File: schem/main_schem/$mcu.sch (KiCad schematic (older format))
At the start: 36 parts, among them P2 CONN_PORTD, P3 CONN_ICD, P4 CONN_NFC, SW1 SW_RESET, U4 25LC256, U5 PIC18F97J60, X1 25MHz

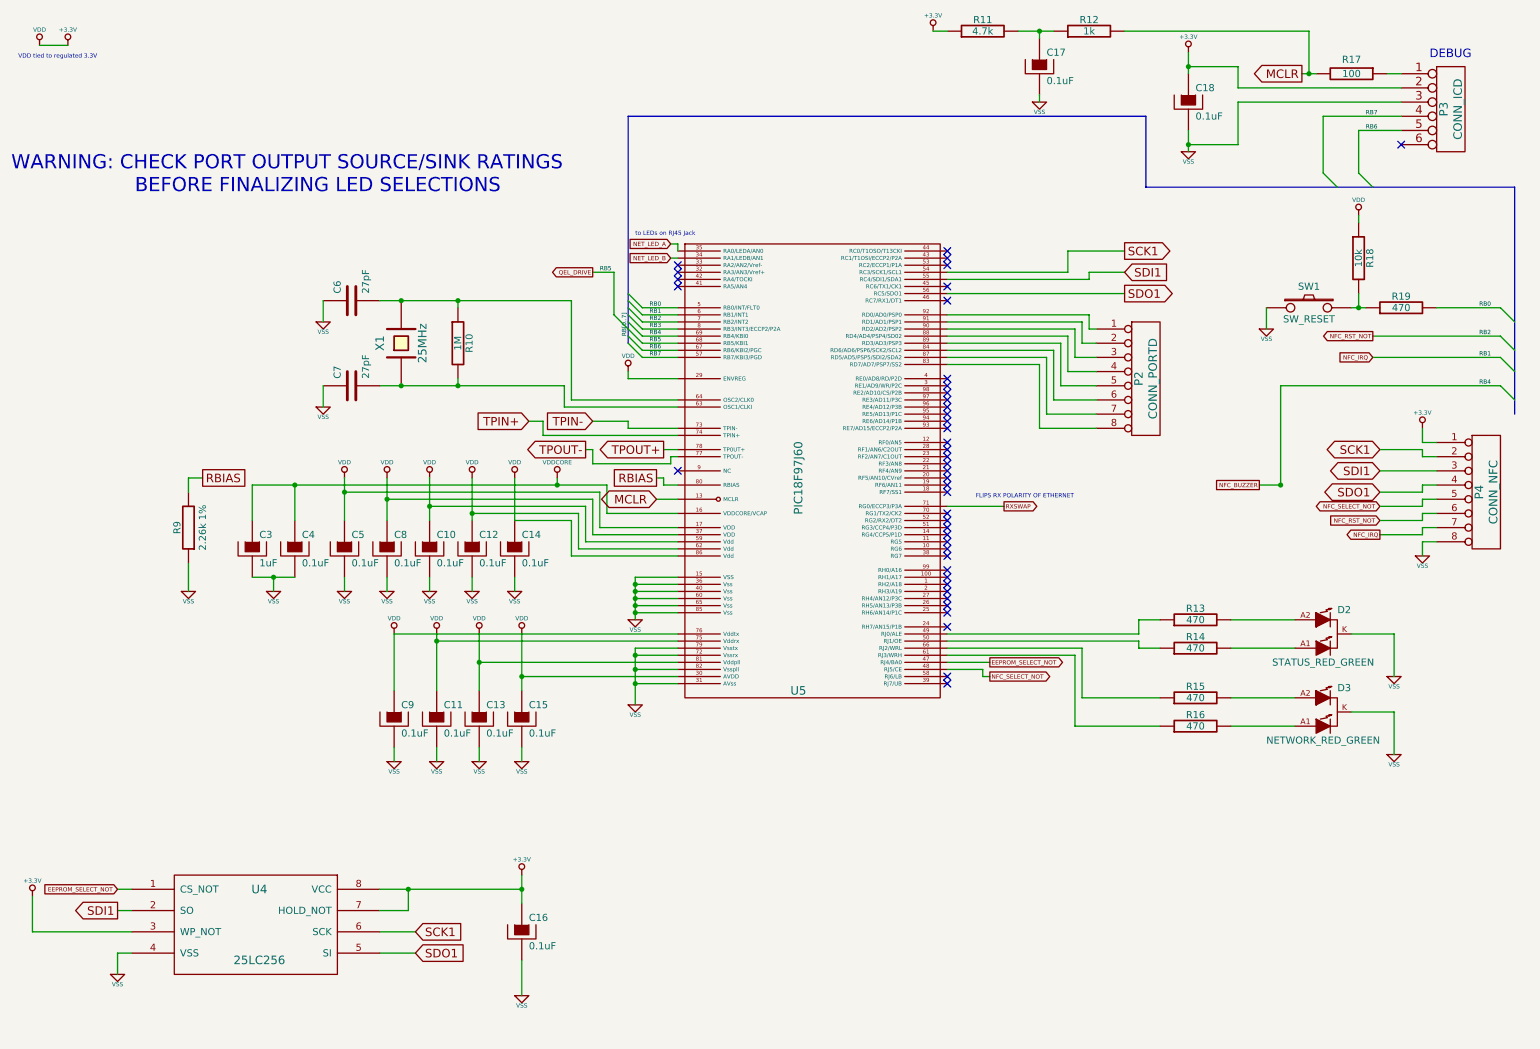
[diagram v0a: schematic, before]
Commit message: Board has own RJ45 jack, finish nearly all logic of board, add QELink screenprint
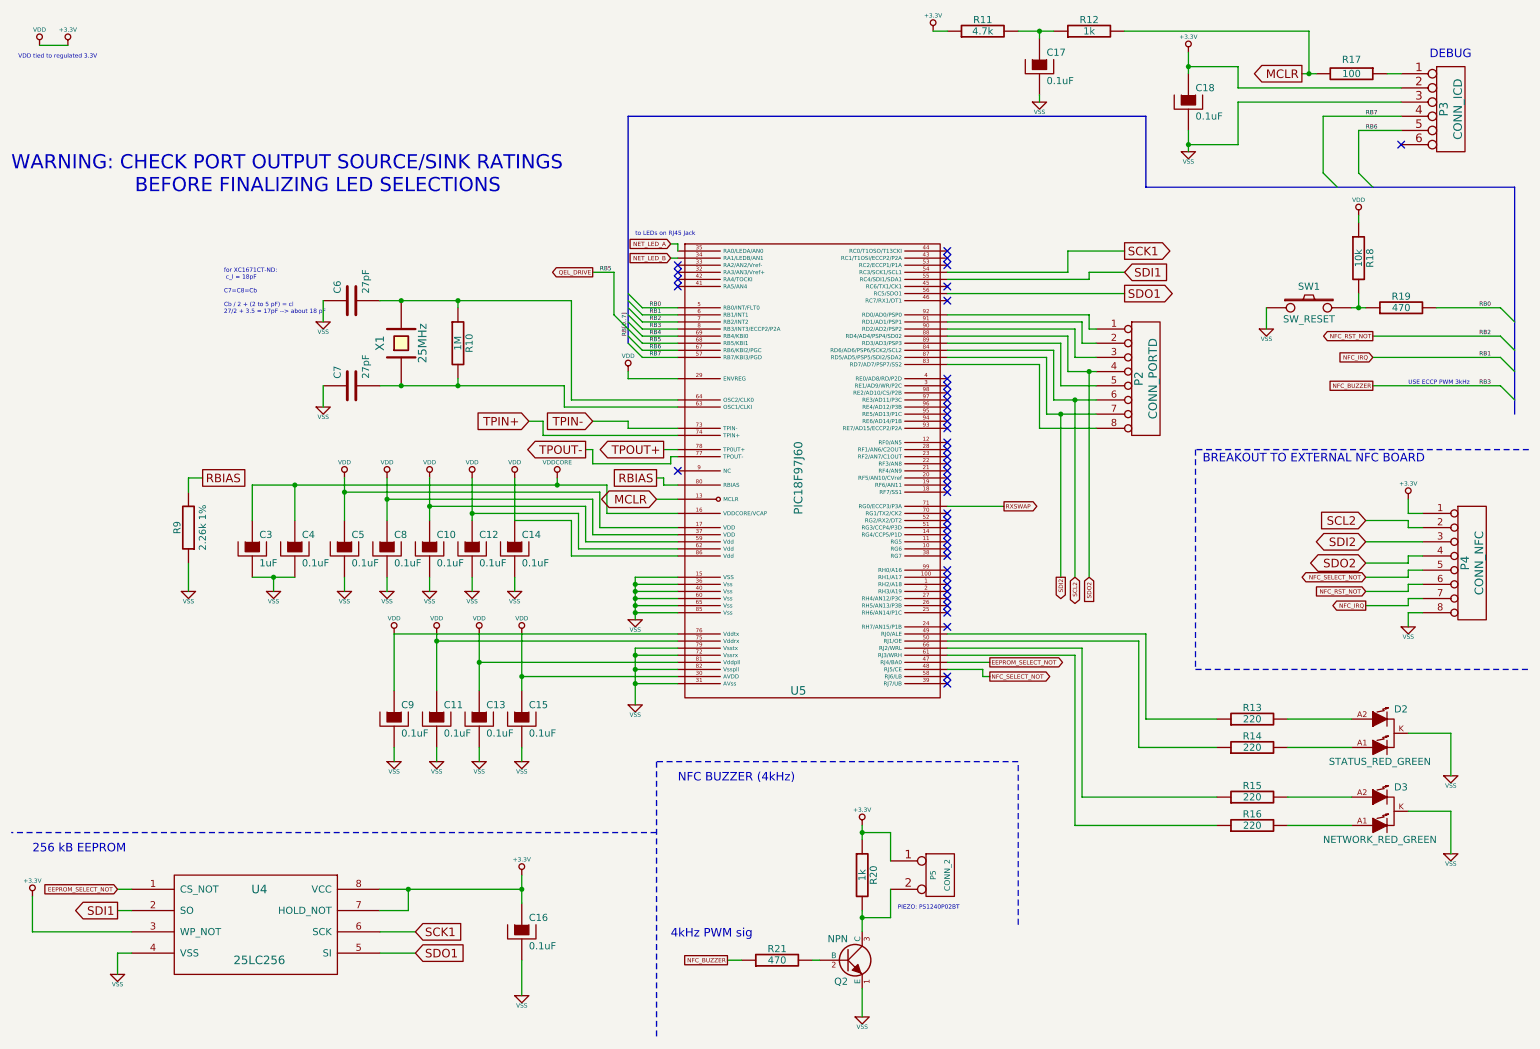
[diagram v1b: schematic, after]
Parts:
- added P5: CONN_2, symbol CONN_2
- added Q2: NPN, symbol NPN
- added R20: 1k, symbol R
- added R21: 470, symbol R
- R13, R14, R15, R16: value 470 -> 220
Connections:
- net RB3 is gone; now on net NFC_BUZZER: U5.8 (RB3/INT3/ECCP2/P2A)
- net +3.3V: now also P5.1 (P1), R20.1
- net NFC_BUZZER: now also R21.1; no longer U5.69 (RB4/KBI0)
- net SCK1: no longer P4.2 (P2)
- net SDI1: no longer P4.3 (P3)
- net SDO1: no longer P4.4 (P4)
- net VSS: now also Q2.1 (E)
- net SCL2: now reaches P2.6 (P6), U5.84 (RD6/AD6/PSP6/SCK2/SCL2)
- net SCL2: now also P4.2 (P2)
- net SDI2: now reaches P2.7 (P7), U5.87 (RD5/AD5/PSP5/SDI2/SDA2)
- net SDI2: now also P4.3 (P3)
- net SDO2: now reaches P2.4 (P4), U5.88 (RD4/AD4/PSP4/SD02)
- net SDO2: now also P4.4 (P4)
- new net: Q2.2 (B), R21.2
- new net: P5.2 (PM), Q2.3 (C), R20.2
- new net RB4: U5.69 (RB4/KBI0)
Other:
- note added: "256 kB EEPROM"
- note added: "4kHz PWM sig"
- note added: "BREAKOUT TO EXTERNAL NFC BOARD"
- note added: "NFC BUZZER (4kHz)"
- note added: "PIEZO: PS1240P02BT"
- note added: "USE ECCP PWM 3kHz"
- note added: "for XC1671CT-ND:\n c_l = 18pF\n\nC7=C8=Cb\n\nCb / 2 + (2 to 5 pF) = cl\n27/2 + 3.5 = 17pF --> about 18 pF"
- note removed: "FLIPS RX POLARITY OF ETHERNET"
- moved on the sheet: D2, D3, P4, R13, R14, R15, R16
